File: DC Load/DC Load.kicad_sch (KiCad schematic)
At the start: 53 parts, among them IC1 OPA277UA, IC2 LTC1046CS8#PBF, IC3 DAC80501MDGST, J1 VSENSE, J2 LOAD_POS, J3 LOAD_NEG, J4 DC 15V..18V, U10 MC7805BD2TR4G, U7 MCP3426, U8 OPA2182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

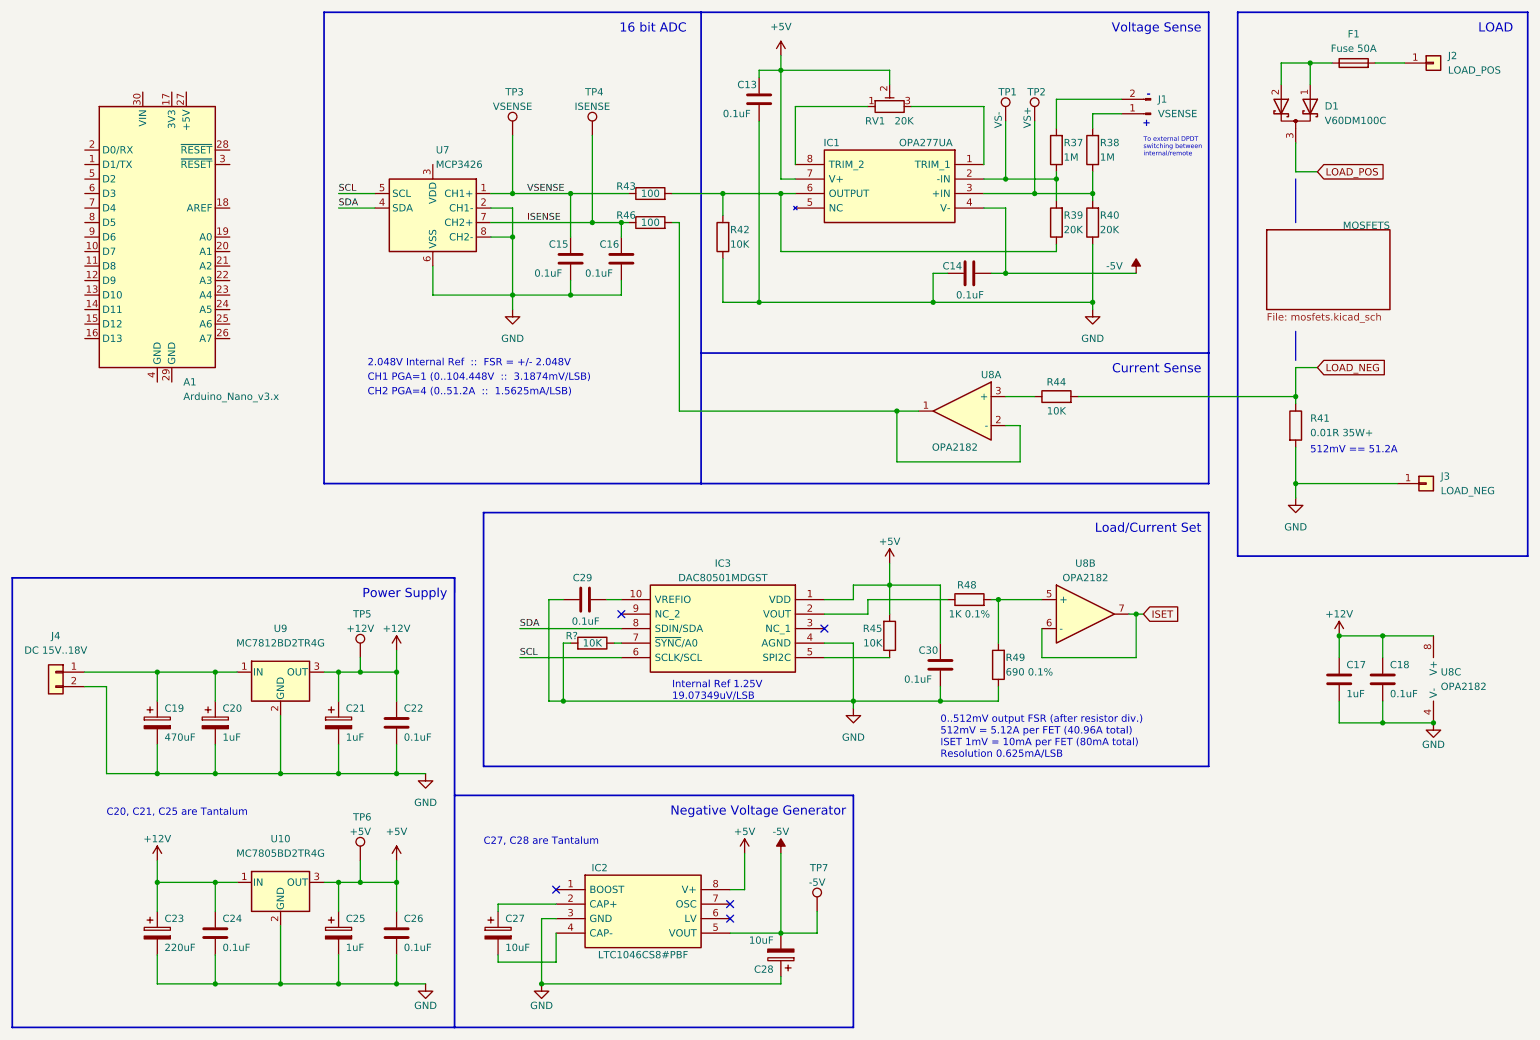
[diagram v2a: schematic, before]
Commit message: Separate sheet for ADC and DAC
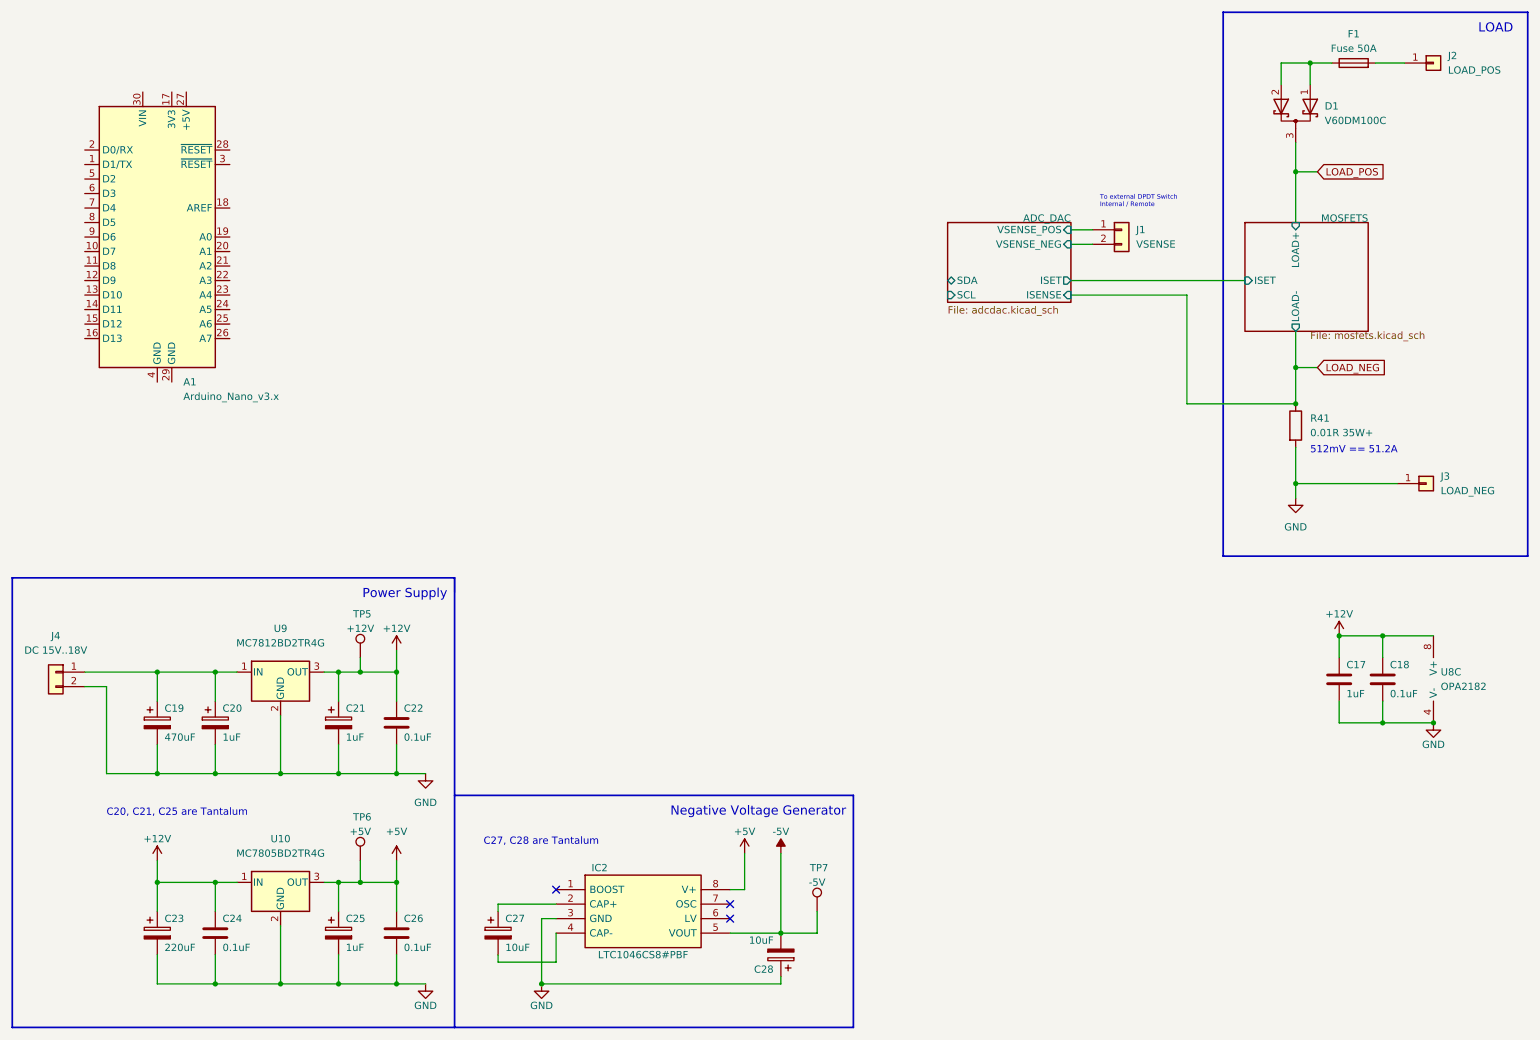
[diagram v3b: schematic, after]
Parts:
- removed C13, C14, C15, C16, C29, C30: 0.1uF, symbol Device:C
- removed IC1: OPA277UA, SOIC127P600X175-8N, symbol SamacSys_Parts:OPA277UA
- removed IC3: DAC80501MDGST, SOP50P490X110-10N, symbol SamacSys_Parts:DAC80501MDGST
- removed J1: VSENSE, symbol Connector:Conn_01x02_Male
- removed R37, R38: 1M, symbol Device:R
- removed R39, R40: 20K, symbol Device:R
- removed R42, R44, R45, R?: 10K, symbol Device:R
- removed R43, R46: 100, symbol Device:R
- removed R48: 1K 0.1%, symbol Device:R
- removed R49: 690 0.1%, symbol Device:R
- removed RV1: 20K, symbol Device:R_Potentiometer_Trim
- removed TP1: VS-, symbol Connector:TestPoint
- removed TP2: VS+, symbol Connector:TestPoint
- removed TP3: VSENSE, symbol Connector:TestPoint
- removed TP4: ISENSE, symbol Connector:TestPoint
- removed U7: MCP3426, symbol Analog_ADC:MCP3426-xSN
- removed unit 2 of U8
- removed unit 1 of U8
- added J1: VSENSE, symbol Connector_Generic:Conn_01x02
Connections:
- new net ADC_DAC/VSENSE_NEG: J1.2 (Pin_2)
- new net ADC_DAC/VSENSE_POS: J1.1 (Pin_1)
- no-connect marks 5 -> 3
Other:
- added sheet ADC_DAC (adcdac.kicad_sch)
- sheet MOSFETS ports: added ISET, LOAD+, LOAD-; removed none
- note added: "To external DPDT Switch Internal / Remote"
- note removed: "+"
- note removed: "-"
- note removed: "0..512mV output FSR (after resistor div.) 512mV = 5.12A per FET (40.96A total) ISET 1mV = 10mA per FET (80mA total) Resolution 0.625mA/LSB"
- note removed: "16 bit ADC"
- note removed: "2.048V Internal Ref :: FSR = +/- 2.048V"
- note removed: "CH1 PGA=1 (0..104.448V :: 3.1874mV/LSB)"
- note removed: "CH2 PGA=4 (0..51.2A :: 1.5625mA/LSB)"
- note removed: "Current Sense"
- note removed: "Internal Ref 1.25V 19.07349uV/LSB"
- note removed: "Load/Current Set"
- note removed: "To external DPDT"
- note removed: "Voltage Sense"
- note removed: "internal/remote"
- note removed: "switching between"

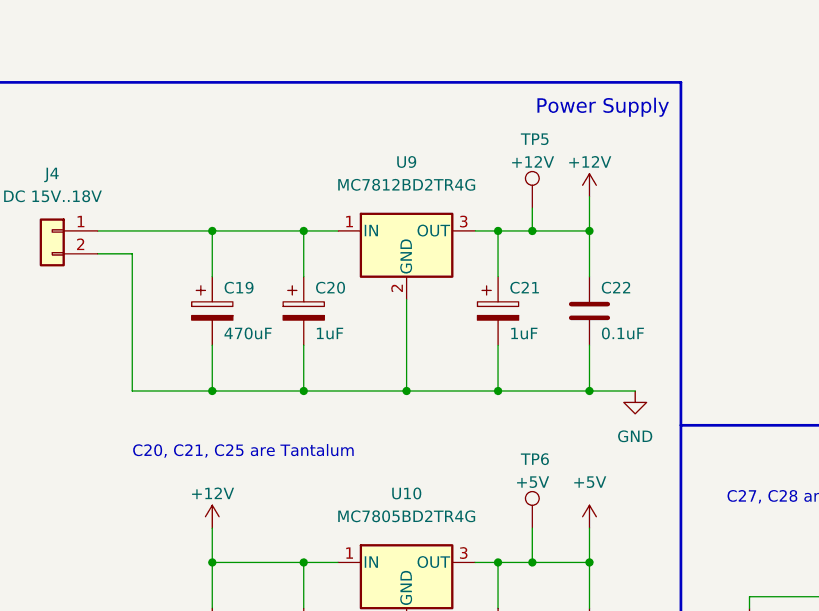
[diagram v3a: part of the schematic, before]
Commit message: Add power flags
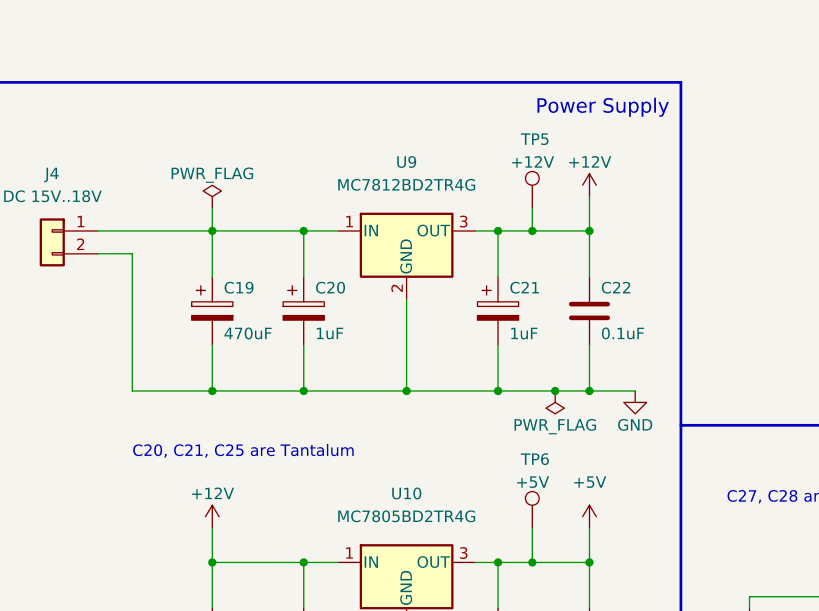
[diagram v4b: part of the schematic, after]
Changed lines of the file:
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@@
   (junction (at 50.8 133.35) (diameter 0) (color 0 0 0 0)
+  )
+  (junction (at 78.74 151.13) (diameter 0) (color 0 0 0 0)
   )
   (junction (at 82.55 133.35) (diameter 0) (color 0 0 0 0)
@@
     (stroke (width 0) (type default) (color 0 0 0 0))
   )
-  (wire (pts (xy 72.39 151.13) (xy 82.55 151.13))
+  (wire (pts (xy 72.39 151.13) (xy 78.74 151.13))
     (stroke (width 0) (type default) (color 0 0 0 0))
   )
@@
     (stroke (width 0) (type default) (color 0 0 0 0))
   )
+  (wire (pts (xy 149.86 165.1) (xy 149.86 179.07))
+    (stroke (width 0) (type default) (color 0 0 0 0))
+  )
   (wire (pts (xy 87.63 151.13) (xy 82.55 151.13))
     (stroke (width 0) (type default) (color 0 0 0 0))
@@
     (stroke (width 0) (type default) (color 0 0 0 0))
   )
+  (wire (pts (xy 78.74 151.13) (xy 82.55 151.13))
+    (stroke (width 0) (type default) (color 0 0 0 0))
+  )
   (wire (pts (xy 240.03 93.98) (xy 240.03 100.33))
     (stroke (width 0) (type default) (color 0 0 0 0))
@@
     (stroke (width 0) (type default) (color 0 0 0 0))
   )
-  (wire (pts (xy 149.86 165.1) (xy 149.86 179.07))
-    (stroke (width 0) (type default) (color 0 0 0 0))
-  )
   (wire (pts (xy 247.65 138.43) (xy 247.65 142.24))
     (stroke (width 0) (type default) (color 0 0 0 0))
@@
   )
   (wire (pts (xy 40.64 151.13) (xy 40.64 146.05))
+    (stroke (width 0) (type default) (color 0 0 0 0))
+  )
+  (wire (pts (xy 40.64 130.81) (xy 40.64 133.35))
     (stroke (width 0) (type default) (color 0 0 0 0))
   )
@@
       (effects (font (size 1.27 1.27)) hide)
     )
-    (property "Value" "GND" (id 1) (at 87.63 156.21 0))
+    (property "Value" "GND" (id 1) (at 87.63 154.94 0))
     (property "Footprint" "" (id 2) (at 87.63 151.13 0)
       (effects (font (size 1.27 1.27)) hide)
     )
     (property "Datasheet" "" (id 3) (at 87.63 151.13 0)
+      (effects (font (size 1.27 1.27)) hide)
+    )
+    (pin "1")
+  )
+  (symbol (lib_id "power:PWR_FLAG") (at 40.64 130.81 0) (unit 1)
+    (in_bom yes) (on_board yes)
+    (property "Reference" "#FLG0102" (id 0) (at 40.64 128.905 0)
+      (effects (font (size 1.27 1.27)) hide)
+    )
+    (property "Value" "PWR_FLAG" (id 1) (at 40.64 127 0))
+    (property "Footprint" "" (id 2) (at 40.64 130.81 0)
+      (effects (font (size 1.27 1.27)) hide)
+    )
+    (property "Datasheet" "~" (id 3) (at 40.64 130.81 0)
       (effects (font (size 1.27 1.27)) hide)
     )
@@
     (pin "1")
   )
+  (symbol (lib_id "power:PWR_FLAG") (at 78.74 151.13 180) (unit 1)
+    (in_bom yes) (on_board yes)
+    (property "Reference" "#FLG0101" (id 0) (at 78.74 153.035 0)
+      (effects (font (size 1.27 1.27)) hide)
+    )
+    (property "Value" "PWR_FLAG" (id 1) (at 78.74 154.94 0))
+    (property "Footprint" "" (id 2) (at 78.74 151.13 0)
+      (effects (font (size 1.27 1.27)) hide)
+    )
+    (property "Datasheet" "~" (id 3) (at 78.74 151.13 0)
+      (effects (font (size 1.27 1.27)) hide)
+    )
+    (pin "1")
+  )
   (symbol (lib_id "Device:C_Polarized") (at 100.33 179.07 0) (unit 1)
     (in_bom yes) (on_board yes)
@@
   )
   (symbol_instances
+    (path "/2b5d11b4-7cb5-41b1-99fe-43653a6eeaaf"
+      (reference "#FLG0101") (unit 1) (value "PWR_FLAG") (footprint "")
+    )
+    (path "/0502644e-e047-4b96-aff3-82b22694f9d8"
+      (reference "#FLG0102") (unit 1) (value "PWR_FLAG") (footprint "")
+    )
     (path "/dbf2ec6d-5b7c-4864-8414-3433d3b742de/1ebd4b8b-44b5-4bb3-b808-459e3ede2288"
       (reference "#PWR01") (unit 1) (value "+12V") (footprint "")
@@
       (reference "#PWR029") (unit 1) (value "GND") (footprint "")
     )
+    (path "/dfd5aec5-c760-49fb-a2c5-6076cb755a00/aad6e91b-812e-485c-a780-1e6007756cf8"
+      (reference "#PWR0101") (unit 1) (value "+5V") (footprint "")
+    )
     (path "/16aec46b-6a38-4237-b970-7429d50e0368"
       (reference "A1") (unit 1) (value "Arduino_Nano_v3.x") (footprint "Module:Arduino_Nano")
@@
       (reference "C8") (unit 1) (value "0.1uF") (footprint "")
     )
+    (path "/dfd5aec5-c760-49fb-a2c5-6076cb755a00/e54c97ab-29d6-421a-a7be-5a9890c1874e"
+      (reference "C9") (unit 1) (value "0.1uF") (footprint "")
+    )
     (path "/dfd5aec5-c760-49fb-a2c5-6076cb755a00/8ae9dc19-cf40-42a2-a0fc-a6f648feb868"

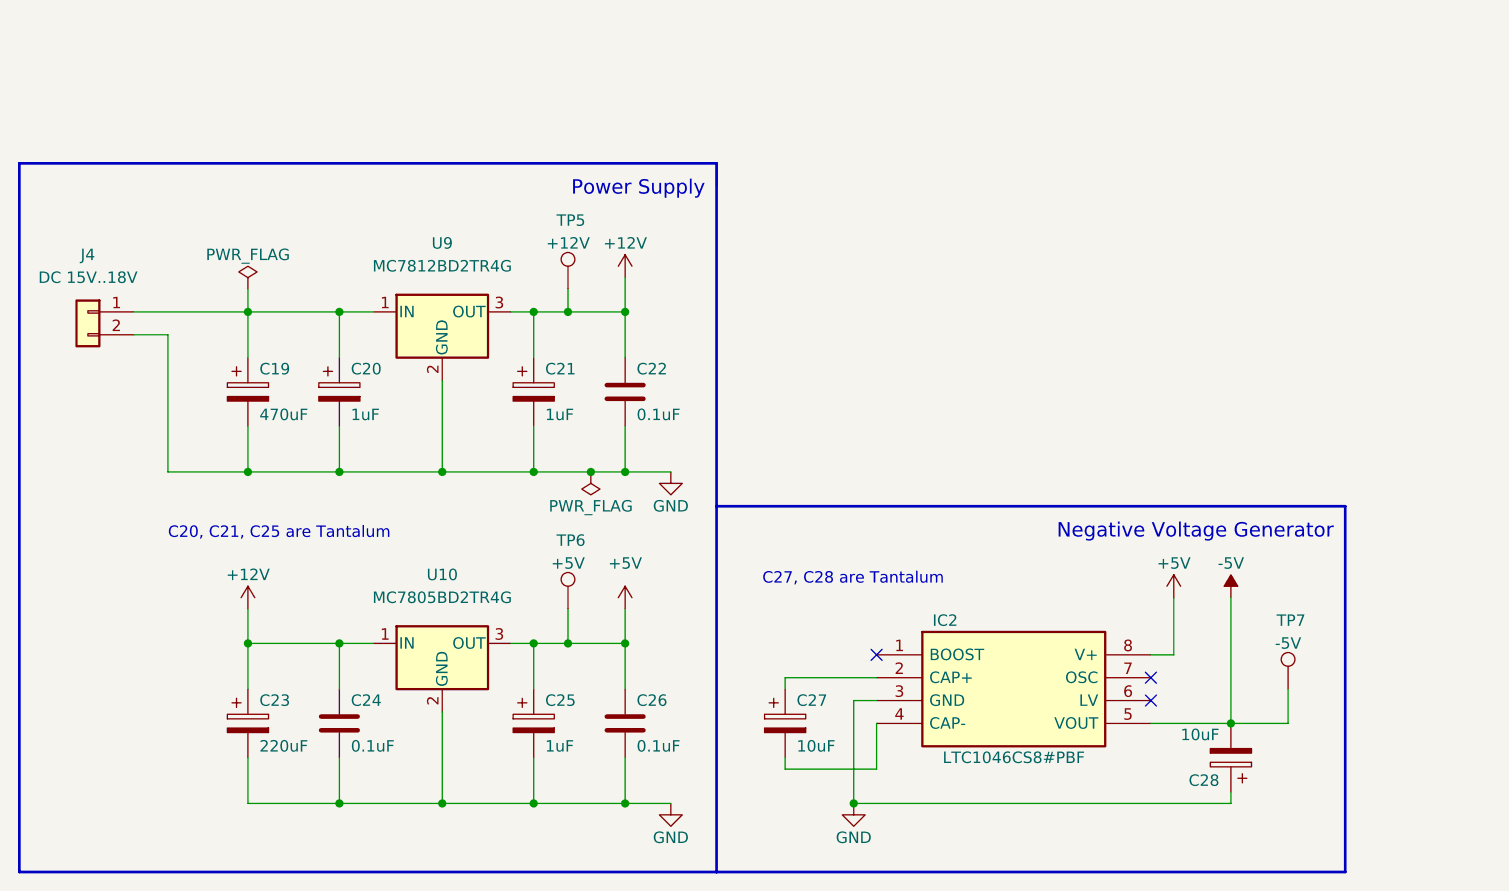
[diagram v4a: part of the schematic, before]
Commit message: Separate sheet for power supply
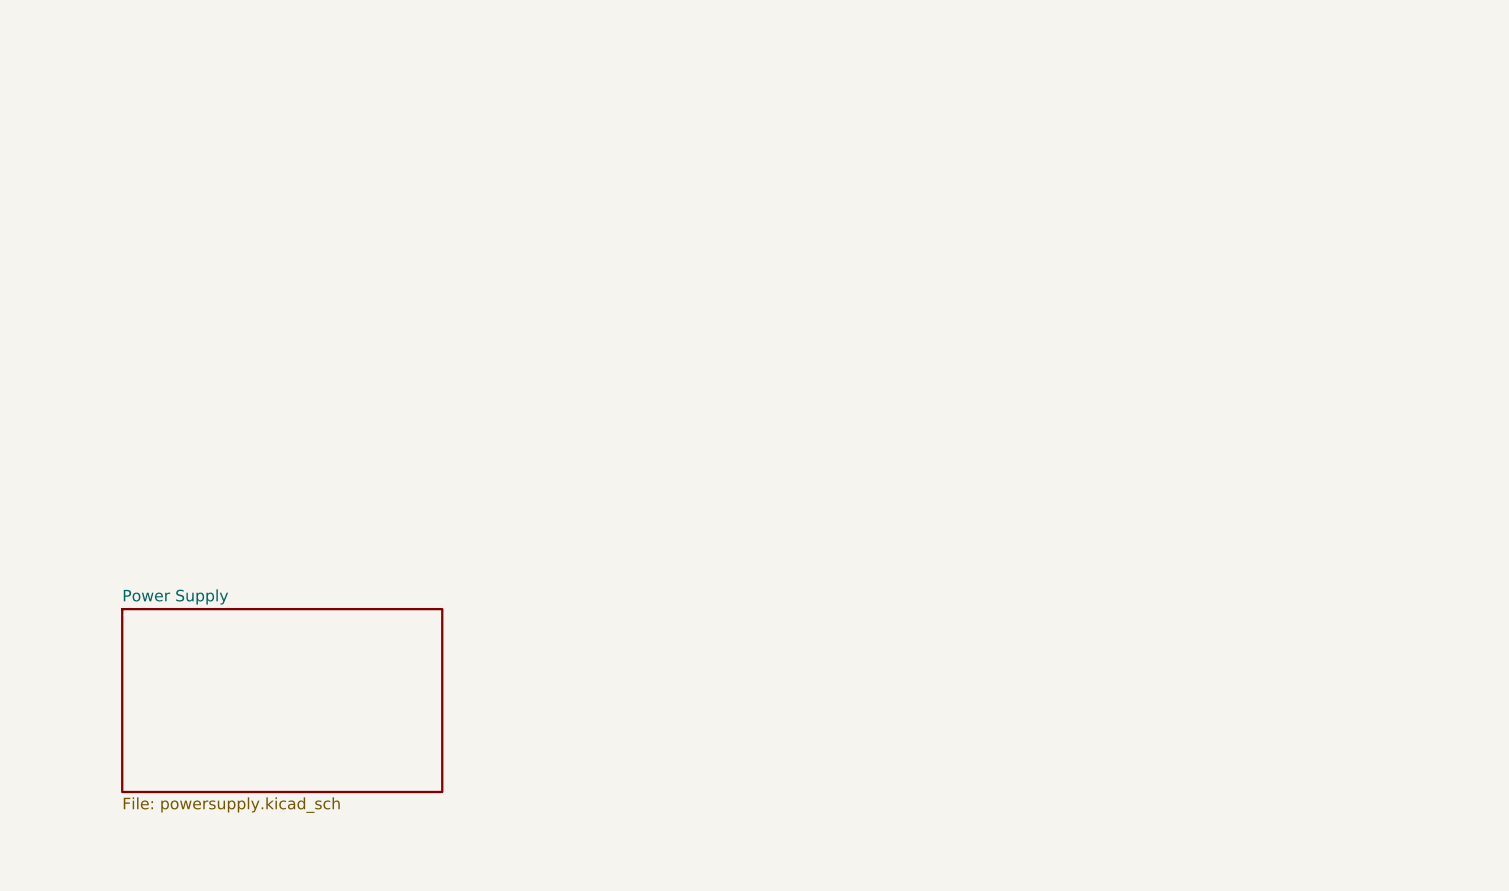
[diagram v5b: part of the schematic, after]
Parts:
- removed C19: 470uF, symbol Device:C_Polarized
- removed C20, C21, C25: 1uF, symbol Device:C_Polarized
- removed C22, C24, C26: 0.1uF, symbol Device:C
- removed C23: 220uF, symbol Device:C_Polarized
- removed C27, C28: 10uF, symbol Device:C_Polarized
- removed IC2: LTC1046CS8#PBF, SOIC127P599X175-8N, symbol SamacSys_Parts:LTC1046CS8#PBF
- removed J4: DC 15V..18V, symbol Connector_Generic:Conn_01x02
- removed TP5: +12V, symbol Connector:TestPoint
- removed TP6: +5V, symbol Connector:TestPoint
- removed TP7: -5V, symbol Connector:TestPoint
- removed U10: MC7805BD2TR4G, Package_TO_SOT_SMD:TO-263-3_TabPin2, symbol Regulator_Linear:L7805
- removed U9: MC7812BD2TR4G, Package_TO_SOT_SMD:TO-263-3_TabPin2, symbol Regulator_Linear:L7812
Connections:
- no-connect marks 3 -> 0
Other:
- added sheet Power Supply (powersupply.kicad_sch)
- note removed: "C20, C21, C25 are Tantalum"
- note removed: "C27, C28 are Tantalum"
- note removed: "Negative Voltage Generator"
- note removed: "Power Supply"

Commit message: update
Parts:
- added U?: STM32F103C8Tx, Package_QFP:LQFP-48_7x7mm_P0.5mm, symbol MCU_ST_STM32F1:STM32F103C8Tx
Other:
- moved on the sheet: R41
